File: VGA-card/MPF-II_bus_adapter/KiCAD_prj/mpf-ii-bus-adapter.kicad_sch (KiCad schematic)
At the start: 32 parts, among them J1 Bus_Apple_II_Card_Side, J10 USER1_Sel, J11 INH_Sel, J12 RDY_Sel, J13 COLREF_Sel, J14 IOSTRB_Sel, J15 Q3_Sel, J16 Pin, J17 Pin, J18 Pin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

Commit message: PCB updated
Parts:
- J1: footprint PCM_MA_Connector_AppleII:Peripheral_Bus_Edge -> PCM_MA_Connector_AppleII:Peripheral_MPFII_Bus_Edge
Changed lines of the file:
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@@
 	(title_block
 		(title "Microprofessor-II Bus Adapter Board")
-		(date "2024-07-21")
+		(date "2024-07-23")
 		(rev "A")
 		(comment 1 "Licensed under CERN-OHL-P V2.0 (https://ohwr.org/cern_ohl_p_v2.txt)")
@@
 			)
 		)
-		(property "Footprint" "PCM_MA_Connector_AppleII:Peripheral_Bus_Edge"
+		(property "Footprint" "PCM_MA_Connector_AppleII:Peripheral_MPFII_Bus_Edge"
 			(at 83.82 52.07 0)
 			(effects

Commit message: Schematics updated
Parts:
- added J27: PWR, Connector_PinHeader_2.54mm:PinHeader_1x02_P2.54mm_Vertical, symbol Connector:Conn_01x02_Pin
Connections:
- net +5V: now also J27.1 (Pin_1)
- net GND: now also J27.2 (Pin_2)
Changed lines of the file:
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@@
 	(wire
 		(pts
+			(xy 25.4 110.49) (xy 30.48 110.49)
+		)
+		(stroke
+			(width 0)
+			(type default)
+		)
+	)
+	(wire
+		(pts
 			(xy 86.36 34.29) (xy 101.6 34.29)
 		)
@@
 		)
 	)
+	(wire
+		(pts
+			(xy 25.4 107.95) (xy 30.48 107.95)
+		)
+		(stroke
+			(width 0)
+			(type default)
+		)
+	)
 	(bus
 		(pts
@@
 		)
 	)
+	(wire
+		(pts
+			(xy 30.48 110.49) (xy 30.48 111.76)
+		)
+		(stroke
+			(width 0)
+			(type default)
+		)
+	)
 	(bus
 		(pts
@@
 		)
 	)
+	(wire
+		(pts
+			(xy 30.48 107.95) (xy 30.48 105.41)
+		)
+		(stroke
+			(width 0)
+			(type default)
+		)
+	)
 	(bus
 		(pts
@@
 	)
 	(symbol
+		(lib_id "power:+5V")
+		(at 30.48 105.41 0)
+		(unit 1)
+		(exclude_from_sim no)
+		(in_bom yes)
+		(on_board yes)
+		(dnp no)
+		(fields_autoplaced yes)
+		(property "Reference" "#PWR017"
+			(at 30.48 109.22 0)
+			(effects
+				(font
+					(size 1.27 1.27)
+				)
+				(hide yes)
+			)
+		)
+		(property "Value" "+5V"
+			(at 30.48 100.33 0)
+			(effects
+				(font
+					(size 1.27 1.27)
+				)
+			)
+		)
+		(property "Footprint" ""
+			(at 30.48 105.41 0)
+			(effects
+				(font
+					(size 1.27 1.27)
+				)
+				(hide yes)
+			)
+		)
+		(property "Datasheet" ""
+			(at 30.48 105.41 0)
+			(effects
+				(font
+					(size 1.27 1.27)
+				)
+				(hide yes)
+			)
+		)
+		(property "Description" "Power symbol creates a global label with name \"+5V\""
+			(at 30.48 105.41 0)
+			(effects
+				(font
+					(size 1.27 1.27)
+				)
+				(hide yes)
+			)
+		)
+		(pin "1"
+		)
+		(instances
+			(project ""
+				(path "/cfc9cf74-9f21-4b66-b98c-dffd14f2b307"
+					(reference "#PWR017")
+					(unit 1)
+				)
+			)
+		)
+	)
+	(symbol
 		(lib_id "power:+12V")
 		(at 101.6 31.75 0)
@@
 	)
 	(symbol
+		(lib_id "Connector:Conn_01x02_Pin")
+		(at 20.32 107.95 0)
+		(unit 1)
+		(exclude_from_sim no)
+		(in_bom yes)
+		(on_board yes)
+		(dnp no)
+		(fields_autoplaced yes)
+		(property "Reference" "J27"
+			(at 20.955 102.87 0)
+			(effects
+				(font
+					(size 1.27 1.27)
+				)
+			)
+		)
+		(property "Value" "PWR"
+			(at 20.955 105.41 0)
+			(effects
+				(font
+					(size 1.27 1.27)
+				)
+			)
+		)
+		(property "Footprint" "Connector_PinHeader_2.54mm:PinHeader_1x02_P2.54mm_Vertical"
+			(at 20.32 107.95 0)
+			(effects
+				(font
+					(size 1.27 1.27)
+				)
+				(hide yes)
+			)
+		)
+		(property "Datasheet" "~"
+			(at 20.32 107.95 0)
+			(effects
+				(font
+					(size 1.27 1.27)
+				)
+				(hide yes)
+			)
+		)
+		(property "Description" "Generic connector, single row, 01x02, script generated"
+			(at 20.32 107.95 0)
+			(effects
+				(font
+					(size 1.27 1.27)
+				)
+				(hide yes)
+			)
+		)
+		(pin "2"
+		)
+		(pin "1"
+		)
+		(instances
+			(project ""
+				(path "/cfc9cf74-9f21-4b66-b98c-dffd14f2b307"
+					(reference "J27")
+					(unit 1)
+				)
+			)
+		)
+	)
+	(symbol
 		(lib_id "74xx:74LS04")
 		(at 134.62 96.52 0)
@@
 					(unit 1)
 				)
+			)
+		)
+	)
+	(symbol
+		(lib_id "power:GND")
+		(at 30.48 111.76 0)
+		(unit 1)
+		(exclude_from_sim no)
+		(in_bom yes)
+		(on_board yes)
+		(dnp no)
+		(fields_autoplaced yes)
+		(property "Reference" "#PWR016"
+			(at 30.48 118.11 0)
+			(effects
+				(font
+					(size 1.27 1.27)
+				)
+				(hide yes)
+			)
+		)
+		(property "Value" "GND"
+			(at 30.48 116.84 0)
+			(effects
+				(font
+					(size 1.27 1.27)
+				)
+			)
+		)
+		(property "Footprint" ""
+			(at 30.48 111.76 0)
+			(effects
+				(font
+					(size 1.27 1.27)
+				)
+				(hide yes)
+			)
+		)
+		(property "Datasheet" ""
+			(at 30.48 111.76 0)
+			(effects
+				(font
+					(size 1.27 1.27)
+				)
+				(hide yes)
+			)
+		)
+		(property "Description" "Power symbol creates a global label with name \"GND\" , ground"
+			(at 30.48 111.76 0)
+			(effects
+				(font
+					(size 1.27 1.27)
+				)
+				(hide yes)
+			)
+		)
+		(pin "1"
+		)
+		(instances
+			(project ""
+				(path "/cfc9cf74-9f21-4b66-b98c-dffd14f2b307"
+					(reference "#PWR016")
+					(unit 1)
+				)

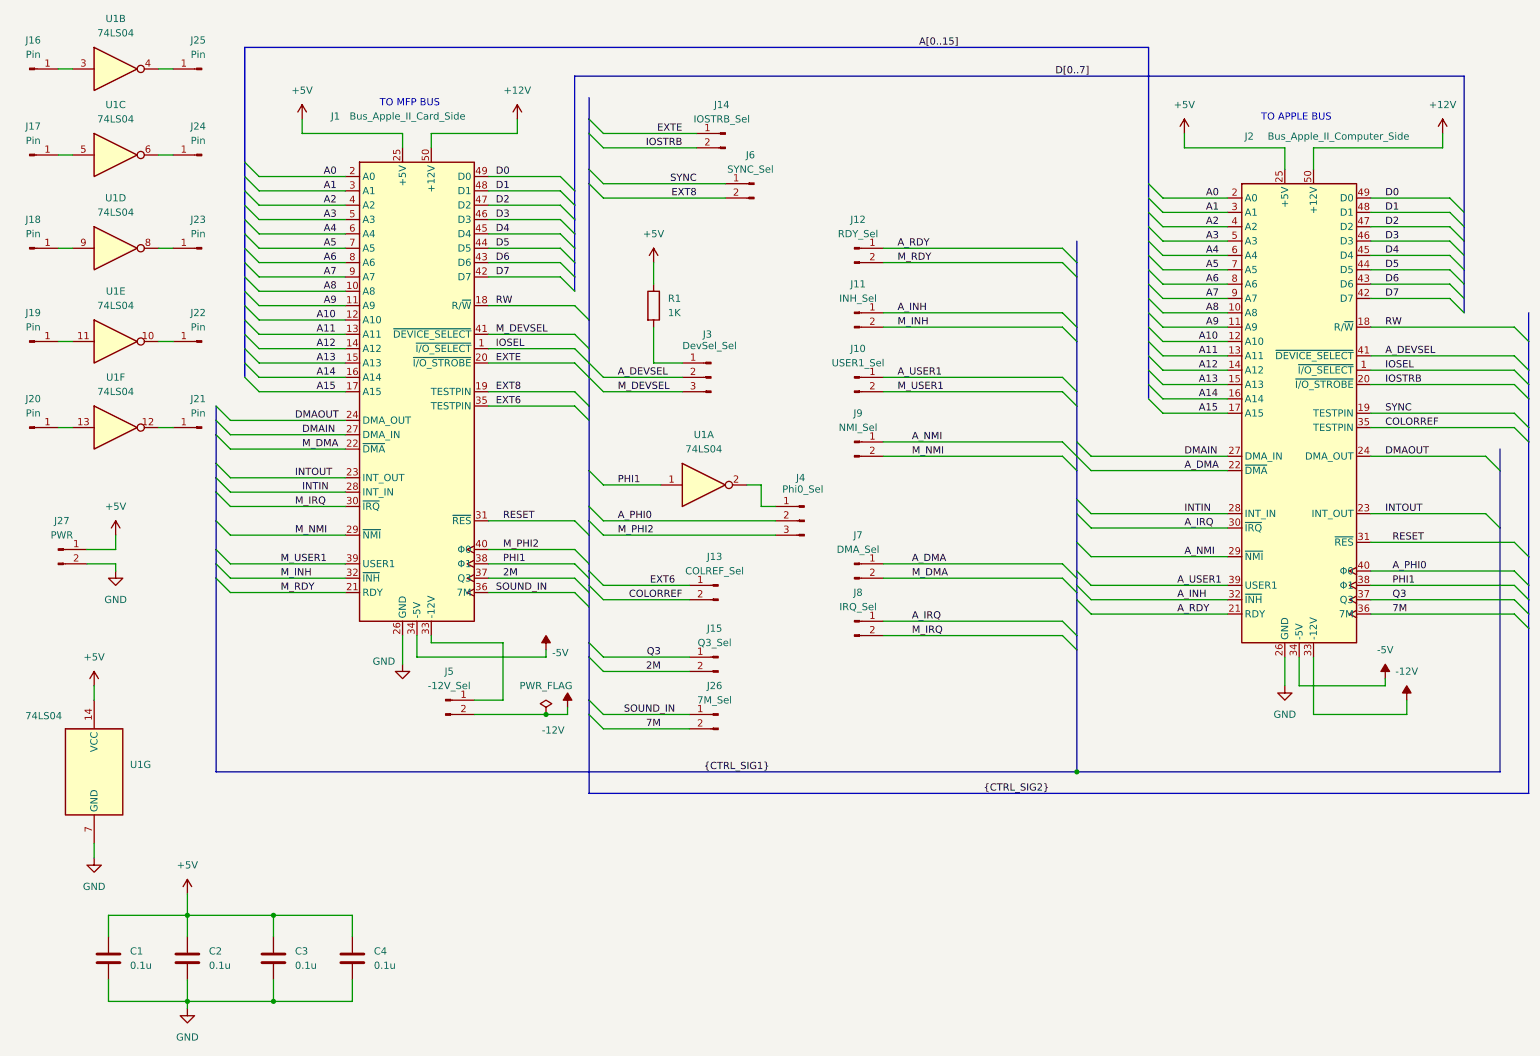
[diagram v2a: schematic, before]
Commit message: Schematics updated with bus pinheader connector
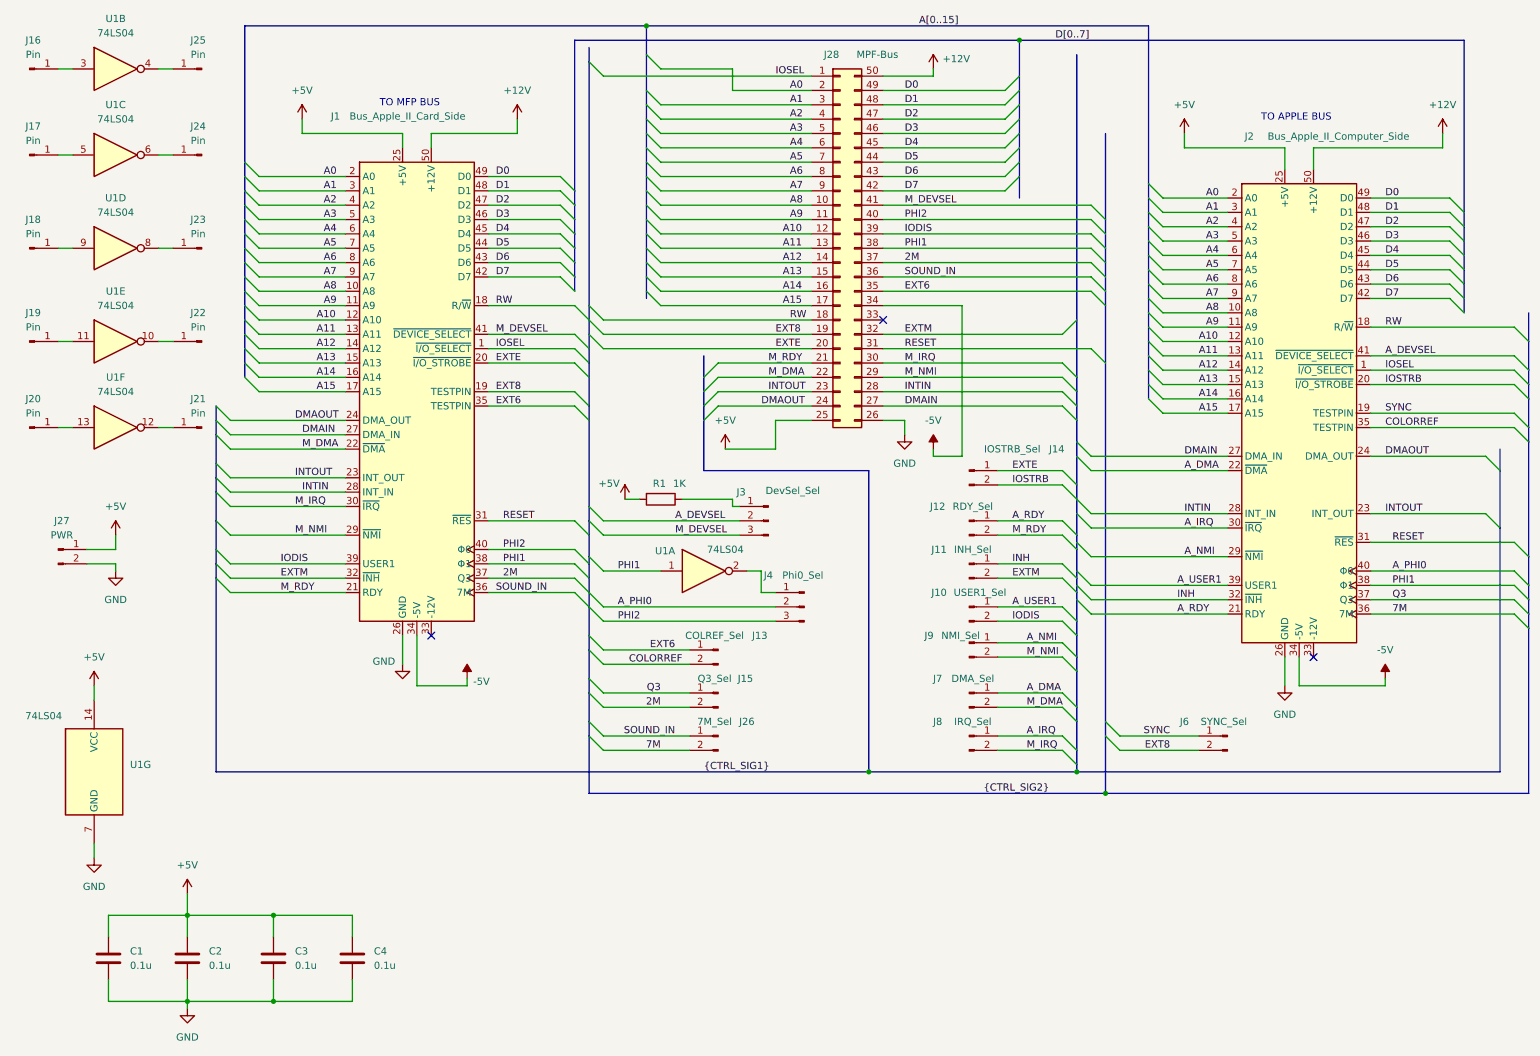
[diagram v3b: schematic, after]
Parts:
- removed J5: -12V_Sel, Connector_PinHeader_2.54mm:PinHeader_1x02_P2.54mm_Vertical, symbol Connector:Conn_01x02_Pin
- added J28: MPF-Bus, Connector_PinHeader_2.54mm:PinHeader_2x25_P2.54mm_Vertical, symbol Connector_Generic:Conn_02x25_Counter_Clockwise
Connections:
- net +12V: now also J28.50 (Pin_50)
- net +5V: now also R1.2, J28.25 (Pin_25); no longer R1.1
- net -5V: now also J28.34 (Pin_34)
- net 2M: now also J28.37 (Pin_37)
- net A0: now also J28.2 (Pin_2)
- net A1: now also J28.3 (Pin_3)
- net A10: now also J28.12 (Pin_12)
- net A11: now also J28.13 (Pin_13)
- net A12: now also J28.14 (Pin_14)
- net A13: now also J28.15 (Pin_15)
- net A14: now also J28.16 (Pin_16)
- net A15: now also J28.17 (Pin_17)
- net A2: now also J28.4 (Pin_4)
- net A3: now also J28.5 (Pin_5)
- net A4: now also J28.6 (Pin_6)
- net A5: now also J28.7 (Pin_7)
- net A6: now also J28.8 (Pin_8)
- net A7: now also J28.9 (Pin_9)
- net A8: now also J28.10 (Pin_10)
- net A9: now also J28.11 (Pin_11)
- net D0: now also J28.49 (Pin_49)
- net D1: now also J28.48 (Pin_48)
- net D2: now also J28.47 (Pin_47)
- net D3: now also J28.46 (Pin_46)
- net D4: now also J28.45 (Pin_45)
- net D5: now also J28.44 (Pin_44)
- net D6: now also J28.43 (Pin_43)
- net D7: now also J28.42 (Pin_42)
- net DMAIN: now also J28.27 (Pin_27)
- net DMAOUT: now also J28.24 (Pin_24)
- net EXT6: now also J28.35 (Pin_35)
- net EXT8: now also J28.19 (Pin_19)
- net EXTE: now also J28.20 (Pin_20)
- net GND: now also J28.26 (Pin_26)
- net INTIN: now also J28.28 (Pin_28)
- net INTOUT: now also J28.23 (Pin_23)
- net IOSEL: now also J28.1 (Pin_1)
- net M_DEVSEL: now also J28.41 (Pin_41)
- net M_DMA: now also J28.22 (Pin_22)
- net M_IRQ: now also J28.30 (Pin_30)
- net M_NMI: now also J28.29 (Pin_29)
- net M_RDY: now also J28.21 (Pin_21)
- net PHI1: now also J28.38 (Pin_38)
- net RESET: now also J28.31 (Pin_31)
- net RW: now also J28.18 (Pin_18)
- net SOUND_IN: now also J28.36 (Pin_36)
- net at J3.1 (Pin_1): now also R1.1; no longer R1.2
- net -12V: no longer names the net of J2.33 (-12V)
- net A_INH renamed INH
- net M_INH renamed EXTM
- net EXTM: now also J28.32 (Pin_32)
- net M_PHI2 renamed PHI2
- net PHI2: now also J28.40 (Pin_40)
- net M_USER1 renamed IODIS
- net IODIS: now also J28.39 (Pin_39)
- no-connect marks 0 -> 3
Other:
- moved on the sheet: J10, J11, J12, J13, J14, J15, J26, J3, J4, J6, J7, J8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

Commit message: New PCB started
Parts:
- added C5: 0.1u, Capacitor_THT:C_Disc_D4.3mm_W1.9mm_P5.00mm, symbol Device:C
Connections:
- net +5V: now also C5.1
- net GND: now also C5.2
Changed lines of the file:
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@@
 	)
 	(junction
+		(at 72.39 187.96)
+		(diameter 0)
+		(color 0 0 0 0)
+	)
+	(junction
 		(at 163.83 147.32)
 		(diameter 0)
@@
 	)
 	(junction
+		(at 72.39 172.72)
+		(diameter 0)
+		(color 0 0 0 0)
+	)
+	(junction
 		(at 124.46 15.24)
 		(diameter 0)
@@
 	(wire
 		(pts
+			(xy 85.09 172.72) (xy 72.39 172.72)
+		)
+		(stroke
+			(width 0)
+			(type default)
+		)
+	)
+	(wire
+		(pts
 			(xy 86.36 36.83) (xy 86.36 34.29)
 		)
@@
 	(wire
 		(pts
+			(xy 85.09 176.53) (xy 85.09 172.72)
+		)
+		(stroke
+			(width 0)
+			(type default)
+		)
+	)
+	(wire
+		(pts
 			(xy 215.9 71.12) (xy 227.33 71.12)
 		)
@@
 		)
 	)
+	(wire
+		(pts
+			(xy 85.09 187.96) (xy 85.09 184.15)
+		)
+		(stroke
+			(width 0)
+			(type default)
+		)
+	)
 	(bus
 		(pts
@@
 		)
 	)
+	(wire
+		(pts
+			(xy 72.39 187.96) (xy 85.09 187.96)
+		)
+		(stroke
+			(width 0)
+			(type default)
+		)
+	)
 	(bus
 		(pts
@@
 					(unit 1)
 				)
+			)
+		)
+	)
+	(symbol
+		(lib_id "Device:C")
+		(at 85.09 180.34 0)
+		(unit 1)
+		(exclude_from_sim no)
+		(in_bom yes)
+		(on_board yes)
+		(dnp no)
+		(fields_autoplaced yes)
+		(property "Reference" "C5"
+			(at 88.9 179.0699 0)
+			(effects
+				(font
+					(size 1.27 1.27)
+				)
+				(justify left)
+			)
+		)
+		(property "Value" "0.1u"
+			(at 88.9 181.6099 0)
+			(effects
+				(font
+					(size 1.27 1.27)
+				)
+				(justify left)
+			)
+		)
+		(property "Footprint" "Capacitor_THT:C_Disc_D4.3mm_W1.9mm_P5.00mm"
+			(at 86.0552 184.15 0)
+			(effects
+				(font
+					(size 1.27 1.27)
+				)
+				(hide yes)
+			)
+		)
+		(property "Datasheet" "~"
+			(at 85.09 180.34 0)
+			(effects
+				(font
+					(size 1.27 1.27)
+				)
+				(hide yes)
+			)
+		)
+		(property "Description" "Unpolarized capacitor"
+			(at 85.09 180.34 0)
+			(effects
+				(font
+					(size 1.27 1.27)
+				)
+				(hide yes)
+			)
+		)
+		(pin "2"
+		)
+		(pin "1"
+		)
+		(instances
+			(project "mpf-ii-bus-adapter"
+				(path "/cfc9cf74-9f21-4b66-b98c-dffd14f2b307"
+					(reference "C5")
+					(unit 1)
+				)

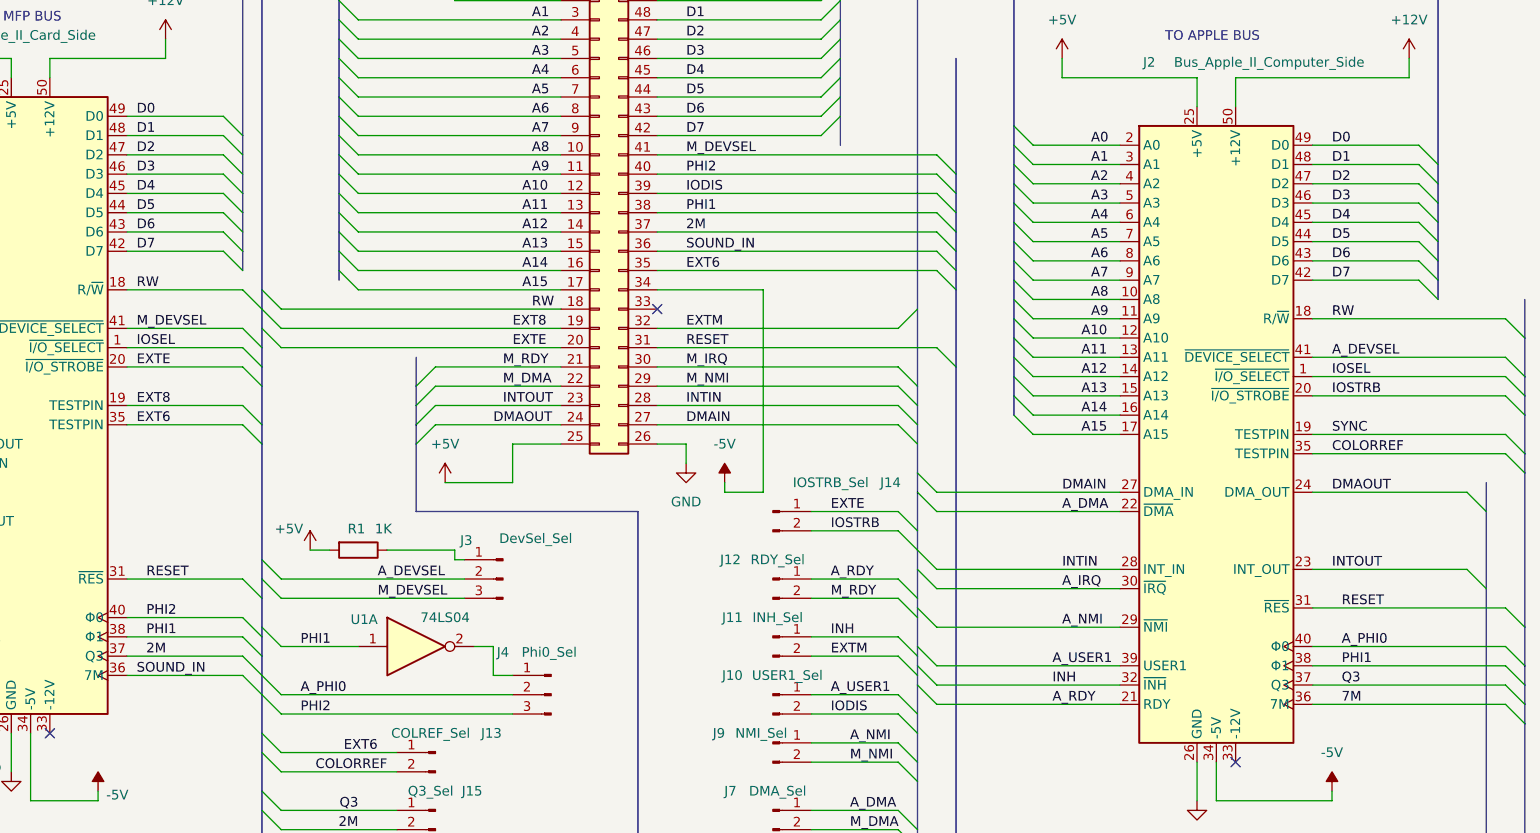
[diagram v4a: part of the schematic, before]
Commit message: Schematics connections list updated
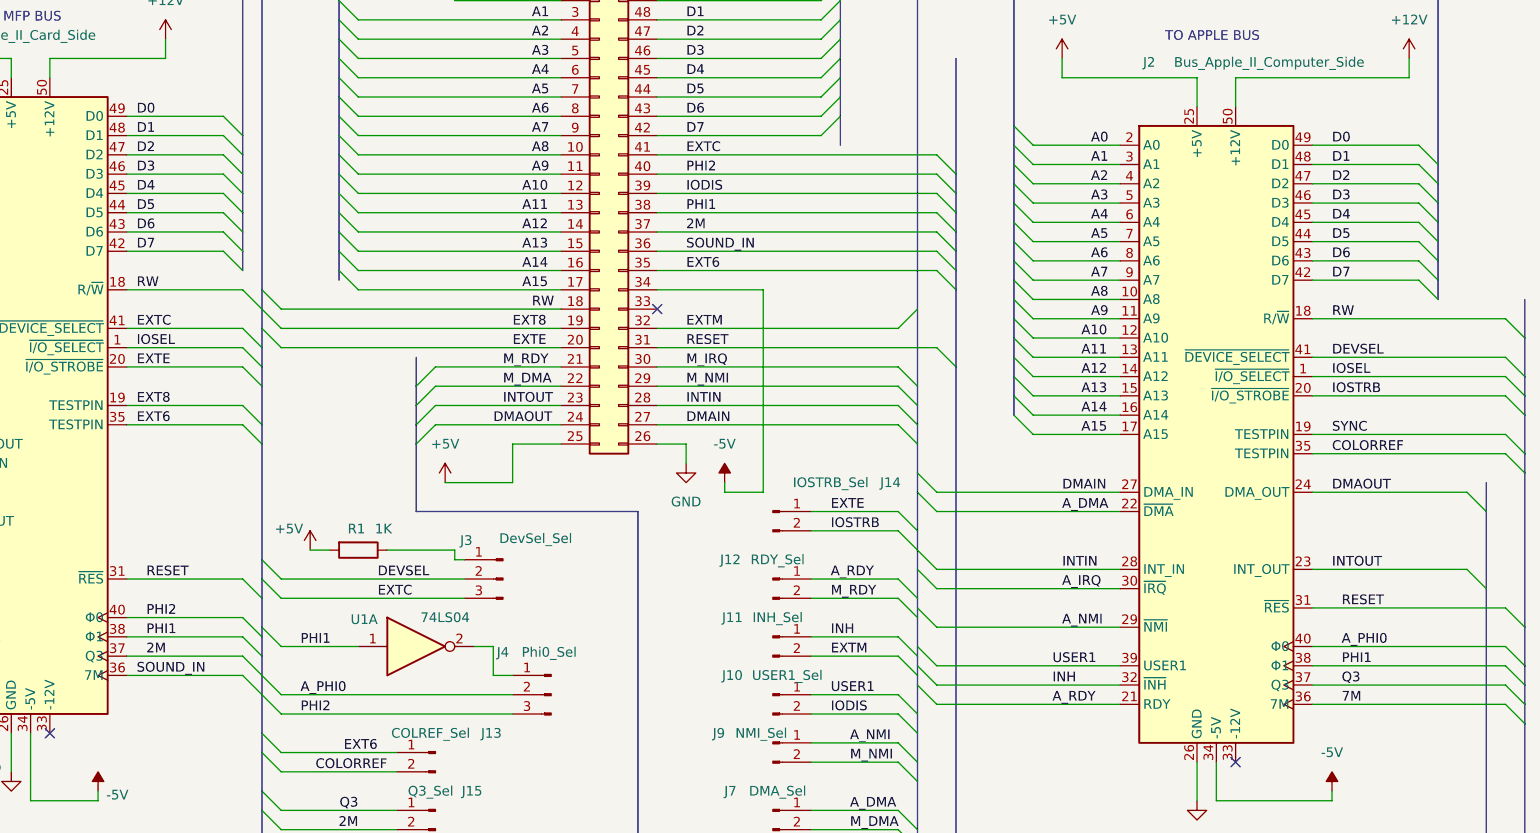
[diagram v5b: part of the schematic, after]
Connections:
- net A_DEVSEL renamed DEVSEL
- net A_USER1 renamed USER1
- net M_DEVSEL renamed EXTC
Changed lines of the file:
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@@
 	(bus_alias "CTRL_SIG1"
 		(members "DMAOUT" "DMAIN" "INTOUT" "INTIN" "M_DMA" "A_DMA" "M_IRQ" "A_IRQ"
-			"M_NMI" "A_NMI" "IODIS" "A_USER1" "EXTM" "INH" "M_RDY" "A_RDY"
+			"M_NMI" "A_NMI" "IODIS" "USER1" "EXTM" "INH" "M_RDY" "A_RDY" "EXTE" "IOSTRB"
 		)
 	)
 	(bus_alias "CTRL_SIG2"
-		(members "RW" "M_DEVSEL" "A_DEVSEL" "IOSEL" "EXTE" "IOSTRB" "EXT8" "EXT6"
-			"COLORREF" "RESET" "PHI1" "PHI2" "A_PHI0" "2M" "Q3" "SOUND_IN" "7M" "SYNC"
+		(members "RW" "EXTC" "DEVSEL" "IOSEL" "EXTE" "IOSTRB" "EXT8" "EXT6" "COLORREF"
+			"RESET" "PHI1" "PHI2" "A_PHI0" "2M" "Q3" "SOUND_IN" "7M" "SYNC"
 		)
 	)
@@
 		)
 	)
-	(label "M_DEVSEL"
+	(label "EXTC"
 		(at 170.18 46.99 0)
 		(fields_autoplaced yes)
@@
 		)
 	)
-	(label "A_USER1"
+	(label "USER1"
 		(at 218.44 114.3 0)
 		(fields_autoplaced yes)
@@
 		)
 	)
-	(label "A_DEVSEL"
+	(label "DEVSEL"
 		(at 129.54 102.87 0)
 		(fields_autoplaced yes)
@@
 		)
 	)
-	(label "M_DEVSEL"
+	(label "EXTC"
 		(at 129.54 105.41 0)
 		(fields_autoplaced yes)
@@
 		)
 	)
-	(label "M_DEVSEL"
+	(label "EXTC"
 		(at 97.79 69.85 0)
 		(fields_autoplaced yes)
@@
 		)
 	)
-	(label "A_DEVSEL"
+	(label "DEVSEL"
 		(at 255.27 73.66 0)
 		(fields_autoplaced yes)
@@
 		)
 	)
-	(label "A_USER1"
+	(label "USER1"
 		(at 189.23 118.11 0)
 		(fields_autoplaced yes)
